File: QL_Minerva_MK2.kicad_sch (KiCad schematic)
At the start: 16 parts, among them J1 Conn_01x02_Pin, J2 Conn_01x05_Pin, U1 Socket to QL, U2 W27C512, U3 PCB8563, U4 GAL16V8, U5 74LS133, Y1 Crystal

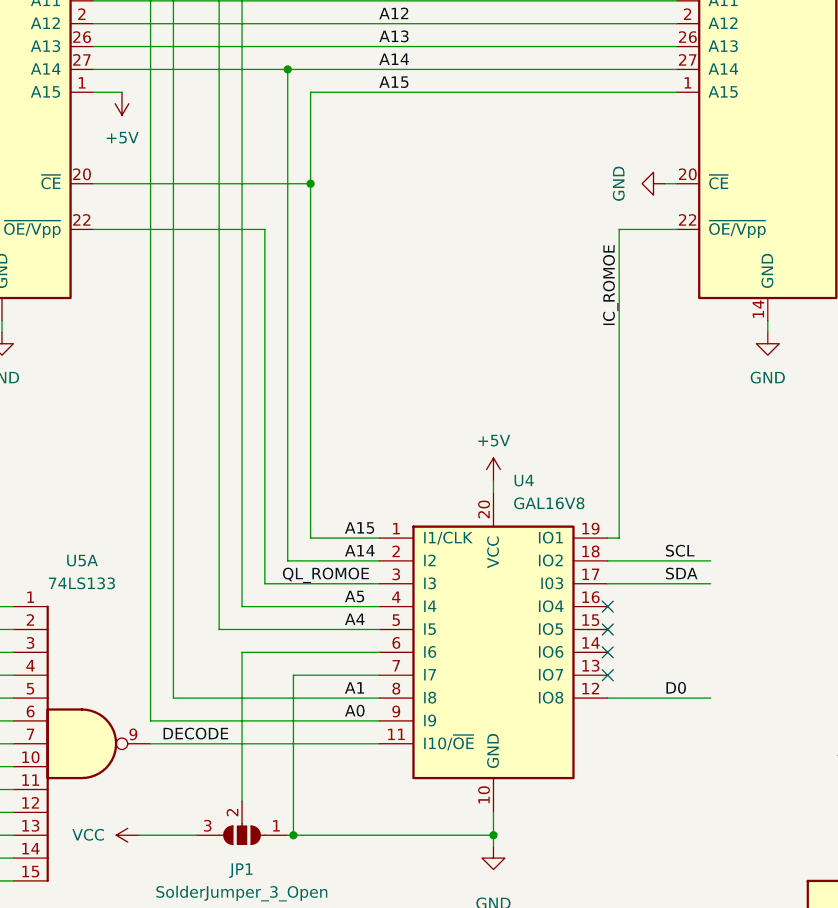
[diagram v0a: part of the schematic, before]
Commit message: update pin 6 of GAL
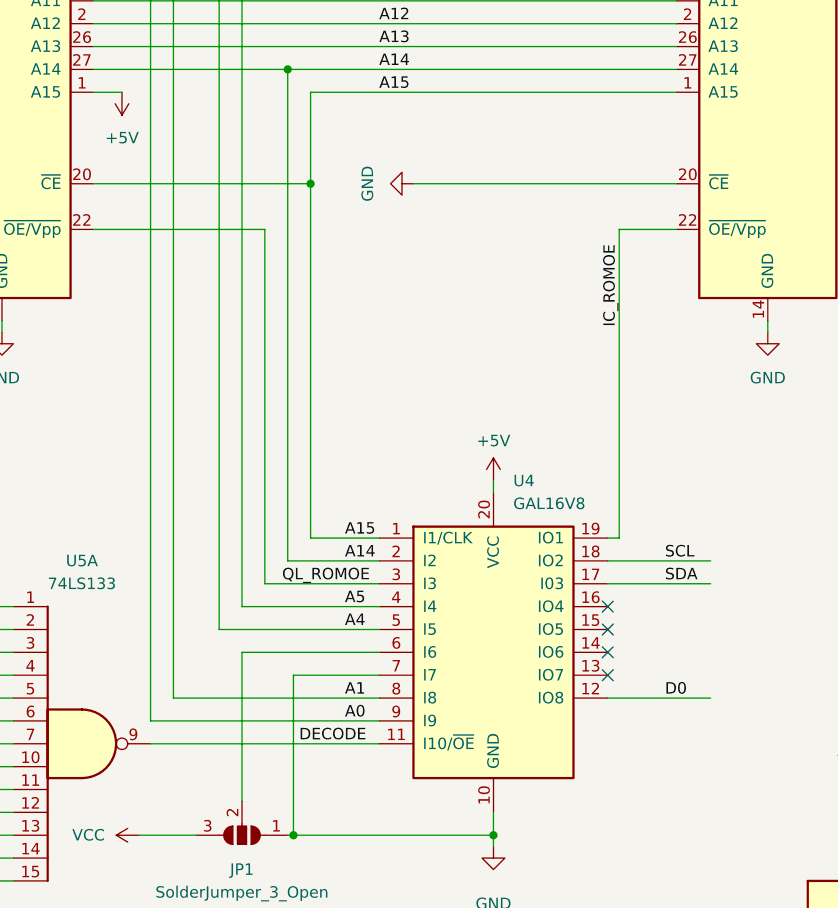
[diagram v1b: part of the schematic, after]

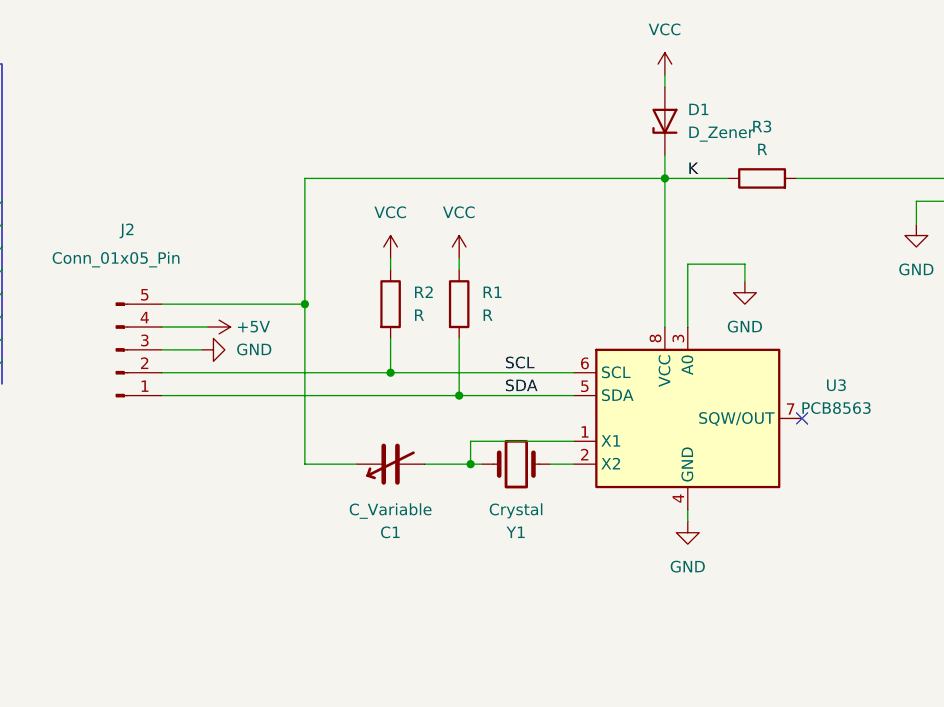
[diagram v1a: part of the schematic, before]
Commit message: add values of components
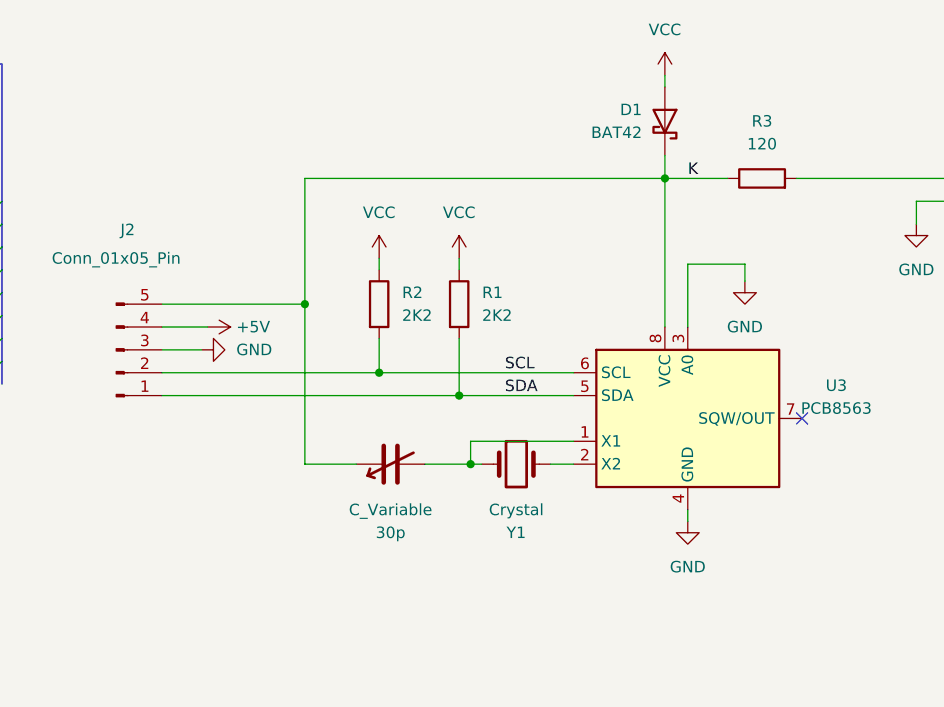
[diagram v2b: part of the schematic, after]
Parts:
- D1: value D_Zener -> BAT42; footprint Diode_THT:D_DO-34_SOD68_P7.62mm_Horizontal -> Diode_THT:D_DO-35_SOD27_P7.62mm_Horizontal; symbol Device:D_Zener -> Diode:BAT42
- R1, R2: value R -> 2K2
- R3: value R -> 120
- renumbered C1 to 30p
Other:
- moved on the sheet: D1, R2
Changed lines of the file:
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@@
   (junction (at 187.325 48.26) (diameter 0) (color 0 0 0 0)
   )
+  (junction (at 195.58 55.88) (diameter 0) (color 0 0 0 0)
+  )
   (junction (at 78.74 87.63) (diameter 0) (color 0 0 0 0)
   )
@@
   )
   (junction (at 227.33 34.29) (diameter 0) (color 0 0 0 0)
-  )
-  (junction (at 196.85 55.88) (diameter 0) (color 0 0 0 0)
   )
   (junction (at 68.58 49.53) (diameter 0) (color 0 0 0 0)
@@
     (stroke (width 0) (type default))
   )
-  (wire (pts (xy 196.85 52.07) (xy 196.85 55.88))
+  (wire (pts (xy 195.58 52.07) (xy 195.58 55.88))
     (stroke (width 0) (type default))
   )
@@
     (stroke (width 0) (type default))
   )
-  (wire (pts (xy 196.85 55.88) (xy 217.17 55.88))
-    (stroke (width 0) (type default))
-  )
   (bus (pts (xy 153.67 39.37) (xy 153.67 41.91))
     (stroke (width 0) (type default))
@@
     (stroke (width 0) (type default))
   )
-  (wire (pts (xy 171.45 55.88) (xy 196.85 55.88))
+  (wire (pts (xy 171.45 55.88) (xy 195.58 55.88))
     (stroke (width 0) (type default))
   )
@@
     (stroke (width 0) (type default))
   )
-  (wire (pts (xy 196.85 43.18) (xy 196.85 44.45))
+  (wire (pts (xy 195.58 55.88) (xy 217.17 55.88))
+    (stroke (width 0) (type default))
+  )
+  (wire (pts (xy 195.58 43.18) (xy 195.58 44.45))
     (stroke (width 0) (type default))
   )
@@
     )
   )
-  (symbol (lib_id "Device:R") (at 196.85 48.26 0) (unit 1)
-    (in_bom yes) (on_board yes) (dnp no) (fields_autoplaced)
-    (property "Reference" "R2" (at 199.39 46.99 0)
+  (symbol (lib_id "Device:R") (at 195.58 48.26 0) (unit 1)
+    (in_bom yes) (on_board yes) (dnp no) (fields_autoplaced)
+    (property "Reference" "R2" (at 198.12 46.99 0)
       (effects (font (size 1.27 1.27)) (justify left))
     )
-    (property "Value" "R" (at 199.39 49.53 0)
+    (property "Value" "2K2" (at 198.12 49.53 0)
       (effects (font (size 1.27 1.27)) (justify left))
     )
-    (property "Footprint" "8bits:R_Axial_DIN0204_L3.6mm_D1.6mm_P11.17mm_Horizontal" (at 195.072 48.26 90)
-      (effects (font (size 1.27 1.27)) hide)
-    )
-    (property "Datasheet" "~" (at 196.85 48.26 0)
+    (property "Footprint" "8bits:R_Axial_DIN0204_L3.6mm_D1.6mm_P11.17mm_Horizontal" (at 193.802 48.26 90)
+      (effects (font (size 1.27 1.27)) hide)
+    )
+    (property "Datasheet" "~" (at 195.58 48.26 0)
       (effects (font (size 1.27 1.27)) hide)
     )
@@
       (effects (font (size 1.27 1.27)) (justify left))
     )
-    (property "Value" "R" (at 207.01 49.53 0)
+    (property "Value" "2K2" (at 207.01 49.53 0)
       (effects (font (size 1.27 1.27)) (justify left))
     )
@@
     )
   )
-  (symbol (lib_id "power:VCC") (at 196.85 43.18 0) (unit 1)
-    (in_bom yes) (on_board yes) (dnp no) (fields_autoplaced)
-    (property "Reference" "#PWR01" (at 196.85 46.99 0)
-      (effects (font (size 1.27 1.27)) hide)
-    )
-    (property "Value" "VCC" (at 196.85 38.1 0)
-      (effects (font (size 1.27 1.27)))
-    )
-    (property "Footprint" "" (at 196.85 43.18 0)
-      (effects (font (size 1.27 1.27)) hide)
-    )
-    (property "Datasheet" "" (at 196.85 43.18 0)
+  (symbol (lib_id "power:VCC") (at 195.58 43.18 0) (unit 1)
+    (in_bom yes) (on_board yes) (dnp no) (fields_autoplaced)
+    (property "Reference" "#PWR01" (at 195.58 46.99 0)
+      (effects (font (size 1.27 1.27)) hide)
+    )
+    (property "Value" "VCC" (at 195.58 38.1 0)
+      (effects (font (size 1.27 1.27)))
+    )
+    (property "Footprint" "" (at 195.58 43.18 0)
+      (effects (font (size 1.27 1.27)) hide)
+    )
+    (property "Datasheet" "" (at 195.58 43.18 0)
       (effects (font (size 1.27 1.27)) hide)
     )
@@
   (symbol (lib_id "Device:R") (at 238.125 34.29 90) (unit 1)
     (in_bom yes) (on_board yes) (dnp no) (fields_autoplaced)
-    (property "Reference" "R3" (at 238.125 28.575 90)
-      (effects (font (size 1.27 1.27)))
-    )
-    (property "Value" "R" (at 238.125 31.115 90)
+    (property "Reference" "R3" (at 238.125 27.94 90)
+      (effects (font (size 1.27 1.27)))
+    )
+    (property "Value" "120" (at 238.125 30.48 90)
       (effects (font (size 1.27 1.27)))
     )
@@
   (symbol (lib_id "Device:C_Variable") (at 196.85 66.04 90) (mirror x) (unit 1)
     (in_bom yes) (on_board yes) (dnp no)
-    (property "Reference" "C1" (at 196.85 73.66 90)
+    (property "Reference" "30p" (at 196.85 73.66 90)
       (effects (font (size 1.27 1.27)))
     )
@@
       (project "QL_Minerva_MK2"
         (path "/0617602b-62d8-4799-89c5-d98fa4eb47c1"
-          (reference "C1") (unit 1)
+          (reference "30p") (unit 1)
         )
       )
@@
     )
   )
-  (symbol (lib_id "Device:D_Zener") (at 227.33 27.94 90) (unit 1)
-    (in_bom yes) (on_board yes) (dnp no) (fields_autoplaced)
-    (property "Reference" "D1" (at 229.87 26.67 90)
+  (symbol (lib_id "Diode:BAT42") (at 227.33 27.94 270) (mirror x) (unit 1)
+    (in_bom yes) (on_board yes) (dnp no)
+    (property "Reference" "D1" (at 224.79 26.67 90)
       (effects (font (size 1.27 1.27)) (justify right))
     )
-    (property "Value" "D_Zener" (at 229.87 29.21 90)
+    (property "Value" "BAT42" (at 224.79 29.21 90)
       (effects (font (size 1.27 1.27)) (justify right))
     )
-    (property "Footprint" "Diode_THT:D_DO-34_SOD68_P7.62mm_Horizontal" (at 227.33 27.94 0)
-      (effects (font (size 1.27 1.27)) hide)
-    )
-    (property "Datasheet" "~" (at 227.33 27.94 0)
-      (effects (font (size 1.27 1.27)) hide)
-    )
+    (property "Footprint" "Diode_THT:D_DO-35_SOD27_P7.62mm_Horizontal" (at 222.885 27.94 0)
+      (effects (font (size 1.27 1.27)) hide)
+    )
+    (property "Datasheet" "http://www.vishay.com/docs/85660/bat42.pdf" (at 227.33 27.94 0)
+      (effects (font (size 1.27 1.27)) hide)
+    )

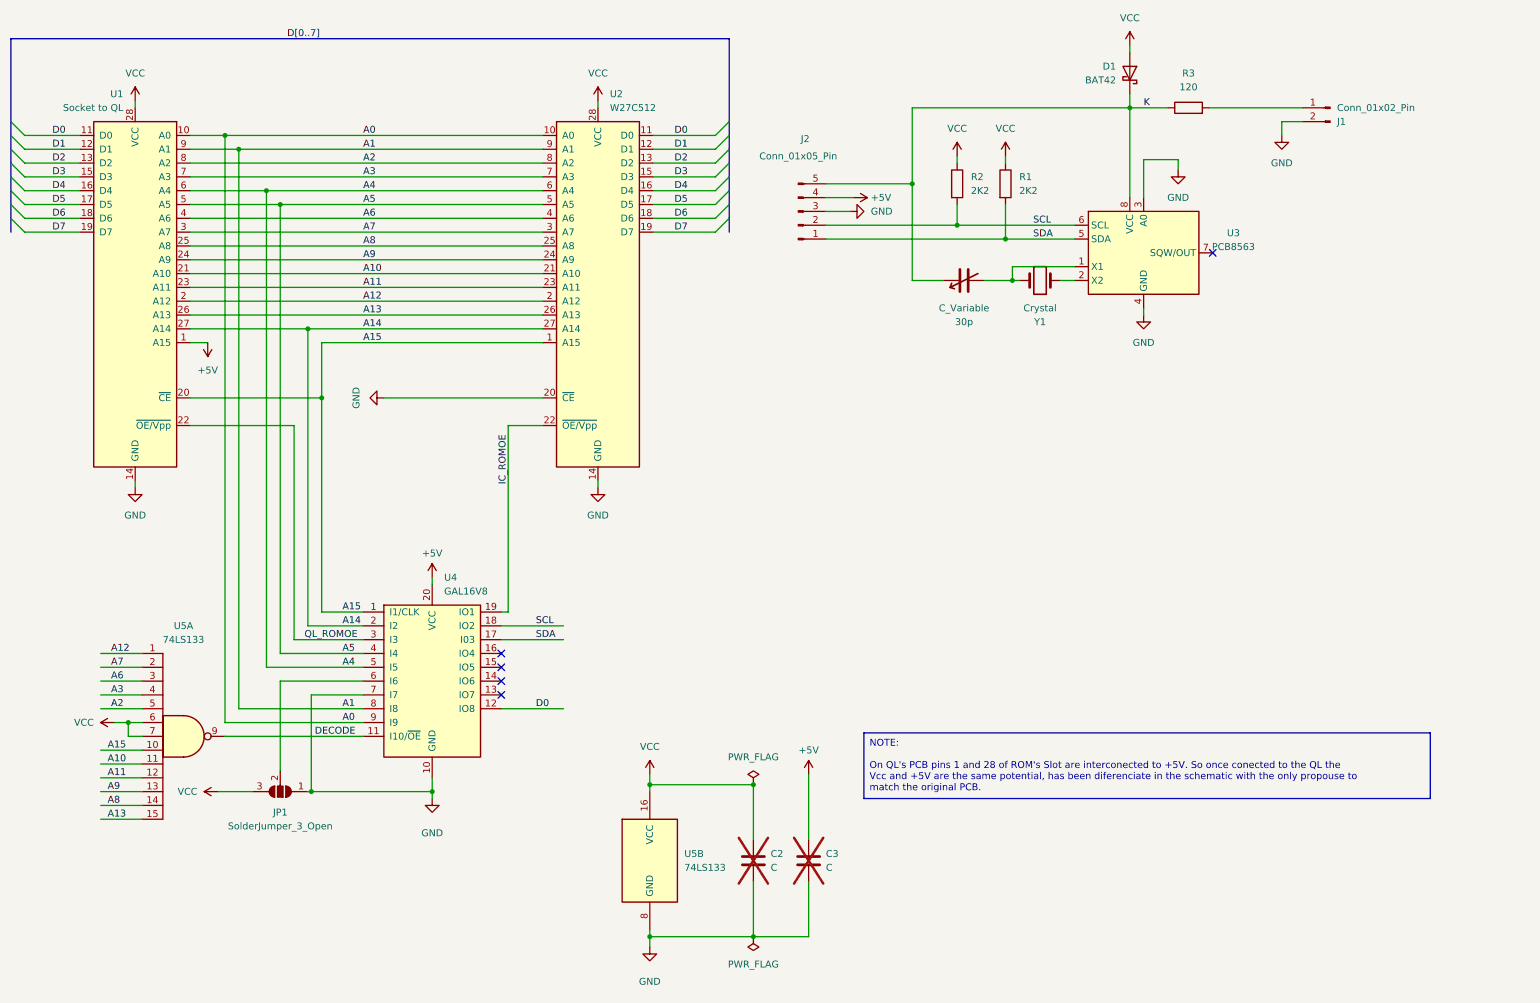
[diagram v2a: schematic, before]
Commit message: Fix references
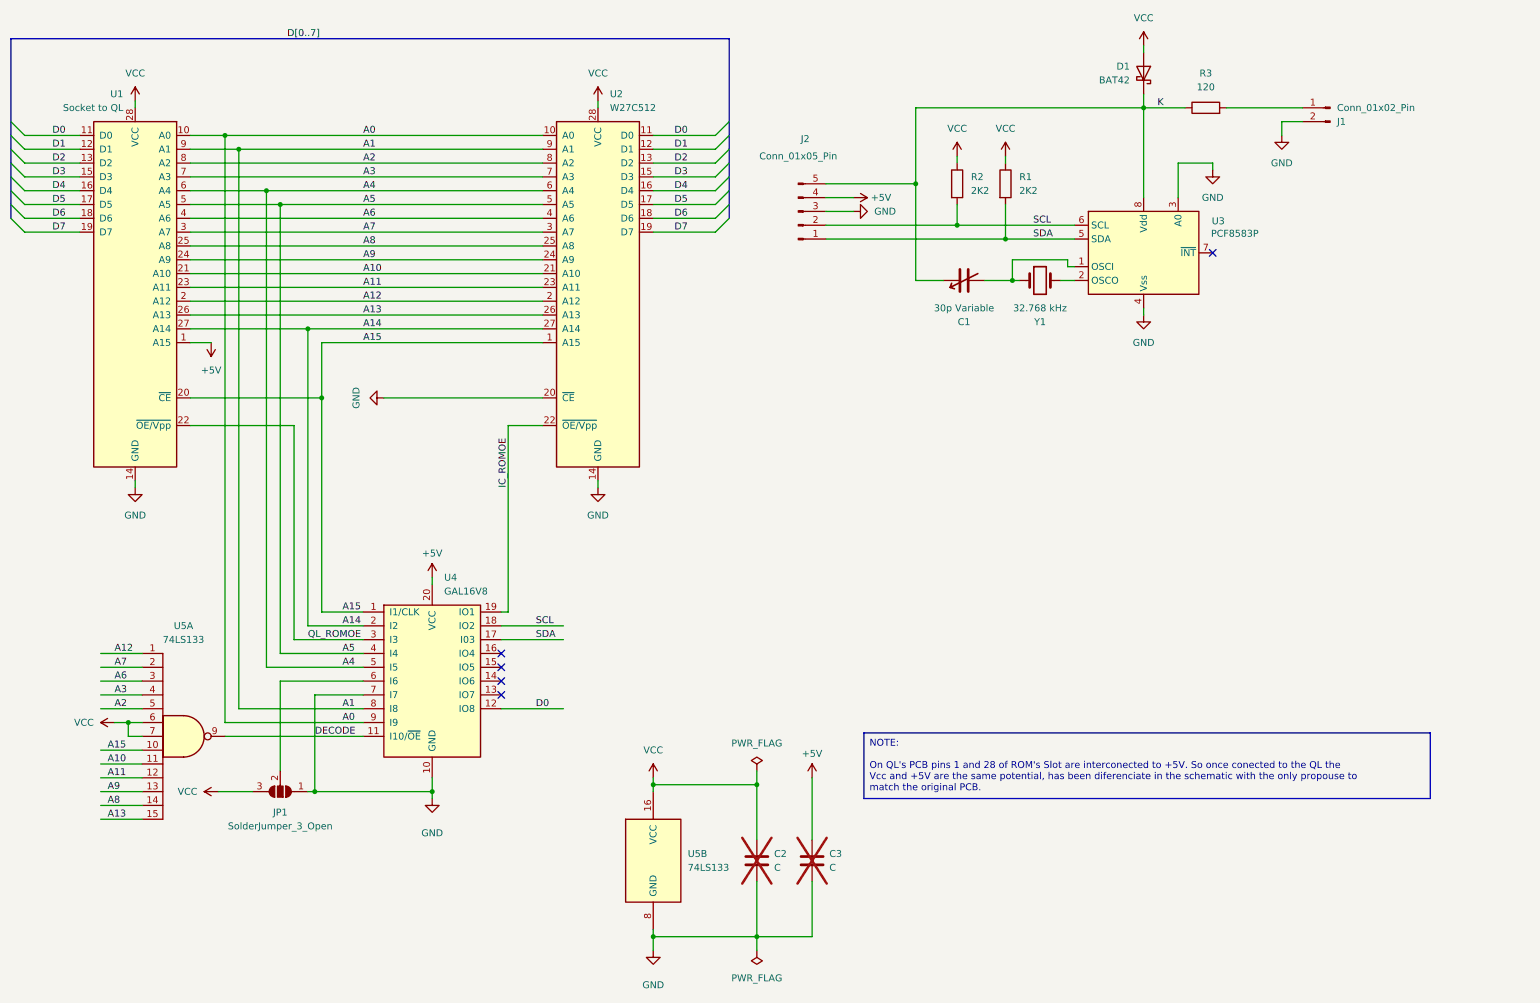
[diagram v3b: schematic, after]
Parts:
- C1: renamed from 30p; value C_Variable -> 30p Variable
- U3: value PCB8563 -> PCF8583P; symbol Timer_RTC:DS1307+ -> 8bits:PCF8583
- Y1: value Crystal -> 32.768 kHz
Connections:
- net DECODE is gone; now on net GND: U4.11 (I10/~{OE}), U5.9
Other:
- moved on the sheet: C2, C3, D1, R3, U5B

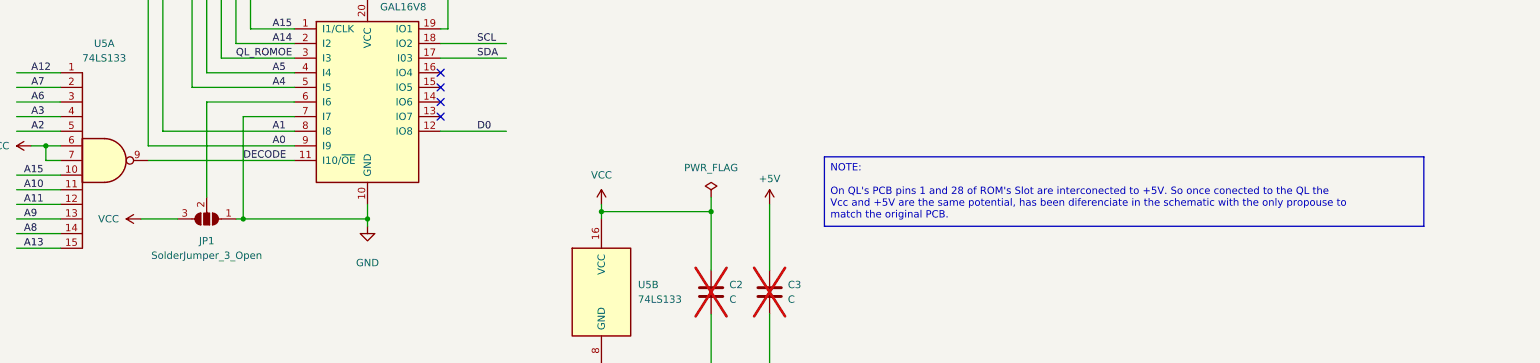
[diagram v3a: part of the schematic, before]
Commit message: update C footprint
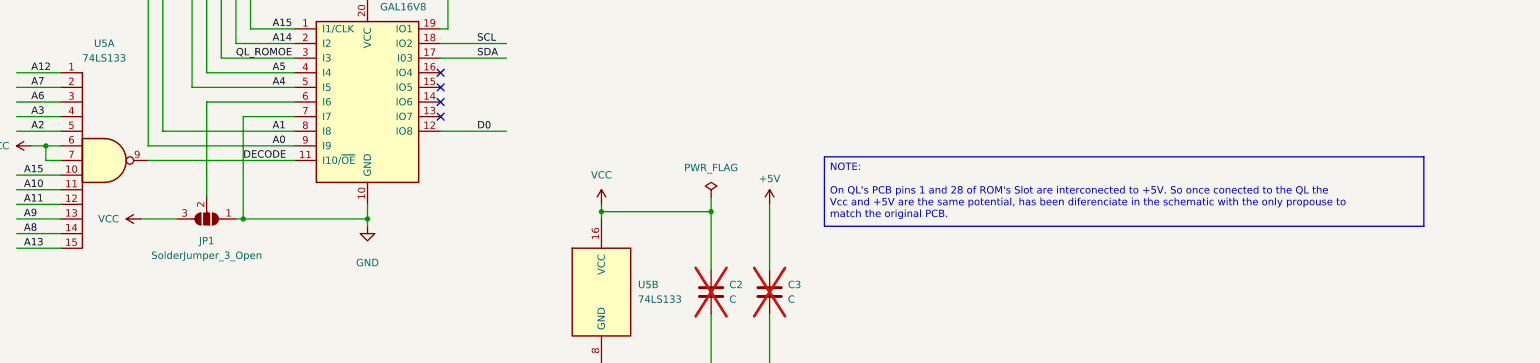
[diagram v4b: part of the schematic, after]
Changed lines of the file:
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@@
 (kicad_sch
-	(version 20231120)
+	(version 20250114)
 	(generator "eeschema")
-	(generator_version "8.0")
+	(generator_version "9.0")
 	(paper "A4")
 	(title_block
@@
 		(company "Alvaro Alea Fernandez")
 	)
+	(text_box "NOTE:\n\nOn QL's PCB pins 1 and 28 of ROM's Slot are interconected to +5V. So once conected to the QL the Vcc and +5V are the same potential, has been diferenciate in the schematic with the only propouse to match the original PCB."
+		(exclude_from_sim no)
+		(at 178.435 149.225 0)
+		(size 104.14 12.065)
+		(margins 0.9525 0.9525 0.9525 0.9525)
+		(stroke
+			(width 0)
+			(type default)
+		)
+		(fill
+			(type none)
+		)
+		(effects
+			(font
+				(size 1.27 1.27)
+			)
+			(justify left top)
+		)
+	)
 	(junction
 		(at 187.96 48.26)
@@
 		)
 	)
-	(text_box "NOTE:\n\nOn QL's PCB pins 1 and 28 of ROM's Slot are interconected to +5V. So once conected to the QL the Vcc and +5V are the same potential, has been diferenciate in the schematic with the only propouse to match the original PCB."
-		(exclude_from_sim no)
-		(at 178.435 149.225 0)
-		(size 104.14 12.065)
-		(stroke
-			(width 0)
-			(type default)
-		)
-		(fill
-			(type none)
-		)
-		(effects
-			(font
-				(size 1.27 1.27)
-			)
-			(justify left top)
-		)
-	)
 	(label "D2"
 		(at 29.21 44.45 0)
@@
 		)
 	)
+	(embedded_fonts no)
 )
